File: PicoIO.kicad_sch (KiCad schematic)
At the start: 14 parts

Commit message: PCB revision 1 (NOT READY FOR USE)
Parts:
- removed J?: Conn_01x07, symbol Connector_Generic:Conn_01x07
- added J12: Conn_01x06, Connector_JST:JST_XH_B6B-XH-A_1x06_P2.50mm_Vertical, symbol Connector_Generic:Conn_01x06
- added R1, R10, R2, R3, R4, R5, R6, R7, R8, R9: 330, Resistor_SMD:R_0805_2012Metric_Pad1.20x1.40mm_HandSolder, symbol Device:R
- J1, J10, J11, J2, J3, J4, J5, J6, J7, J8, J9: renamed from J?; footprint (none) -> Connector_JST:JST_XH_B3B-XH-A_1x03_P2.50mm_Vertical
- J13: renamed from J?; footprint (none) -> Connector_PinHeader_2.54mm:PinHeader_1x03_P2.54mm_Vertical
- U1: renamed from U?; footprint RPi_Pico:RPi_Pico_SMD_TH -> MCU_RaspberryPi_and_Boards:RPi_Pico_SMD_TH
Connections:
- net EXP1 is gone; now on net P1 UR LED: U1.16 (GPIO12)
- net EXP2 is gone; now on net P1 UR: U1.17 (GPIO13)
- net EXP3 is gone; now on net GND: U1.29 (GPIO22)
- net +3V3: now also J12.3 (Pin_3)
- net +5V: now also J12.2 (Pin_2)
- net GND: now also J1.1 (Pin_1), J10.1 (Pin_1), J11.1 (Pin_1), J13.1 (Pin_1), J2.1 (Pin_1), J3.1 (Pin_1), J4.1 (Pin_1), J5.1 (Pin_1), J6.1 (Pin_1), J7.1 (Pin_1), J8.1 (Pin_1), J9.1 (Pin_1), U1.42 (GND), J12.1 (Pin_1); no longer J1.3 (Pin_3), J10.3 (Pin_3), J11.3 (Pin_3), J13.2 (Pin_2), J2.3 (Pin_3), J3.3 (Pin_3), J4.3 (Pin_3), J5.3 (Pin_3), J6.3 (Pin_3), J7.3 (Pin_3), J8.3 (Pin_3), J9.3 (Pin_3)
- net P1 CN: now also J3.3 (Pin_3), U1.12 (GPIO9); no longer J3.1 (Pin_1), U1.14 (GPIO10)
- net P1 CN LED: now also U1.11 (GPIO8), R3.1; no longer J3.2 (Pin_2), U1.15 (GPIO11)
- net P1 DL: now also J1.3 (Pin_3), U1.2 (GPIO1); no longer J1.1 (Pin_1), U1.25 (GPIO19)
- net P1 DL LED: now also U1.1 (GPIO0), R1.1; no longer J1.2 (Pin_2), U1.24 (GPIO18)
- net P1 DR: now also J5.3 (Pin_3), U1.26 (GPIO20); no longer J5.1 (Pin_1), U1.11 (GPIO8)
- net P1 DR LED: now also U1.27 (GPIO21), R5.1; no longer J5.2 (Pin_2), U1.12 (GPIO9)
- net P1 UL: now also J2.3 (Pin_3), U1.7 (GPIO5); no longer J2.1 (Pin_1), U1.27 (GPIO21)
- net P1 UL LED: now also U1.6 (GPIO4), R2.1; no longer J2.2 (Pin_2), U1.26 (GPIO20)
- net P1 UR: now also J4.3 (Pin_3); no longer J4.1 (Pin_1), U1.9 (GPIO6)
- net P1 UR LED: now also R4.1; no longer J4.2 (Pin_2), U1.10 (GPIO7)
- net P2 CN: now also J8.3 (Pin_3), U1.15 (GPIO11); no longer J8.1 (Pin_1), U1.4 (GPIO2)
- net P2 CN LED: now also U1.14 (GPIO10), R8.1; no longer J8.2 (Pin_2), U1.5 (GPIO3)
- net P2 DL: now also J6.3 (Pin_3), U1.5 (GPIO3); no longer J6.1 (Pin_1), U1.22 (GPIO17)
- net P2 DL LED: now also U1.4 (GPIO2), R6.1; no longer J6.2 (Pin_2), U1.21 (GPIO16)
- net P2 DR: now also J10.3 (Pin_3), U1.24 (GPIO18); no longer J10.1 (Pin_1), U1.6 (GPIO4)
- net P2 DR LED: now also U1.25 (GPIO19), R10.1; no longer J10.2 (Pin_2), U1.7 (GPIO5)
- net P2 UL: now also J7.3 (Pin_3), U1.10 (GPIO7); no longer J7.1 (Pin_1), U1.32 (GPIO27_ADC1)
- net P2 UL LED: now also U1.9 (GPIO6), R7.1; no longer J7.2 (Pin_2), U1.31 (GPIO26_ADC0)
- net P2 UR: now also J9.3 (Pin_3), U1.20 (GPIO15); no longer J9.1 (Pin_1), U1.1 (GPIO0)
- net P2 UR LED: now also U1.19 (GPIO14), R9.1; no longer J9.2 (Pin_2), U1.2 (GPIO1)
- net SERVICE: now also J11.3 (Pin_3), U1.21 (GPIO16); no longer J11.2 (Pin_2), U1.19 (GPIO14)
- net SWCLK: now also J13.2 (Pin_2), U1.41 (SWCLK); no longer J13.1 (Pin_1)
- net SWDIO: now also U1.43 (SWDIO)
- net TEST: now also J11.2 (Pin_2), U1.22 (GPIO17); no longer J11.1 (Pin_1), U1.20 (GPIO15)
- net EXP4 renamed ADC2
- net ADC2: now also J12.6 (Pin_6)
- new net: J8.2 (Pin_2), R8.2
- new net: J5.2 (Pin_2), R5.2
- new net: J7.2 (Pin_2), R7.2
- new net: J4.2 (Pin_2), R4.2
- new net: J10.2 (Pin_2), R10.2
- new net: J9.2 (Pin_2), R9.2
- new net: J6.2 (Pin_2), R6.2
- new net: J3.2 (Pin_2), R3.2
- new net: J1.2 (Pin_2), R1.2
- new net: J2.2 (Pin_2), R2.2
- new net ADC0: J12.4 (Pin_4), U1.31 (GPIO26_ADC0)
- new net ADC1: J12.5 (Pin_5), U1.32 (GPIO27_ADC1)
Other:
- moved on the sheet: J10, J11, J13, J6, J7, J8, J9

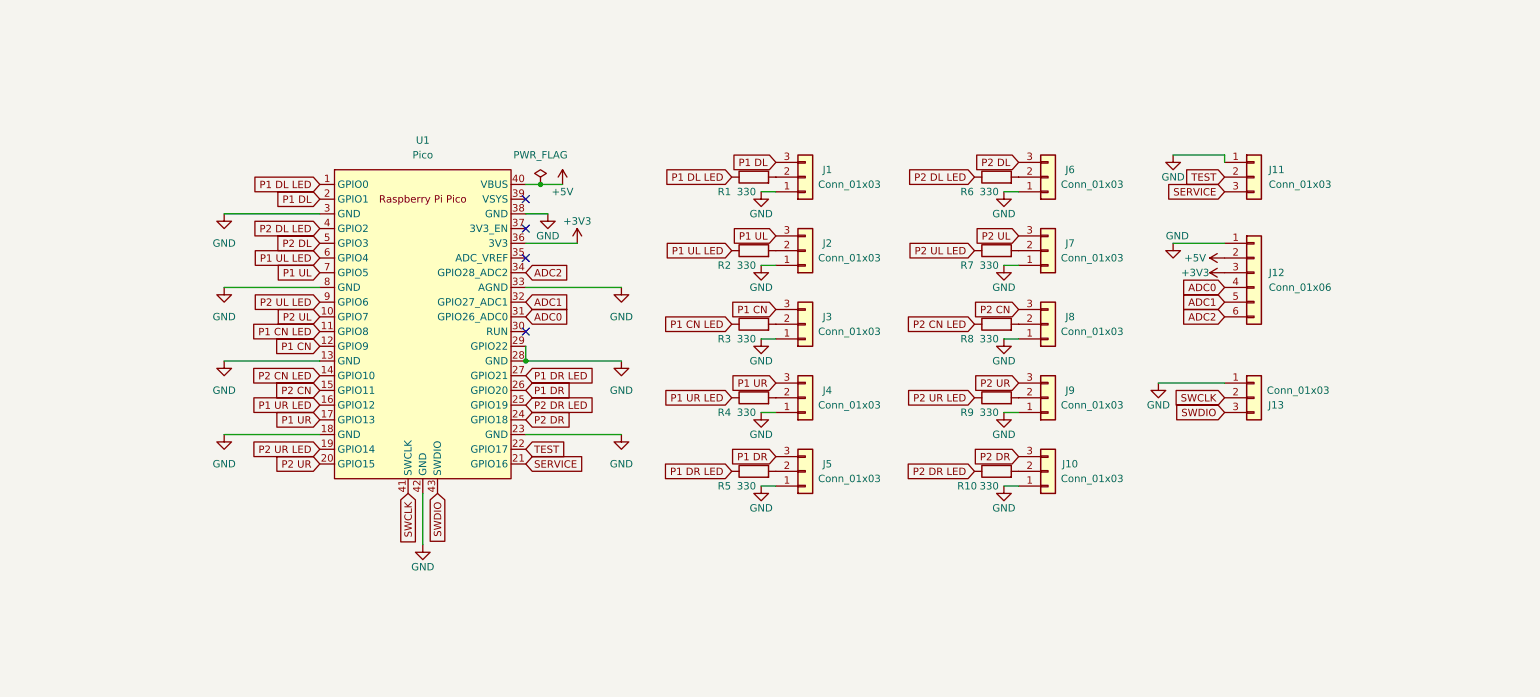
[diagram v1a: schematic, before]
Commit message: Add MOSFETs, move to 4 pin JST, DRC passed
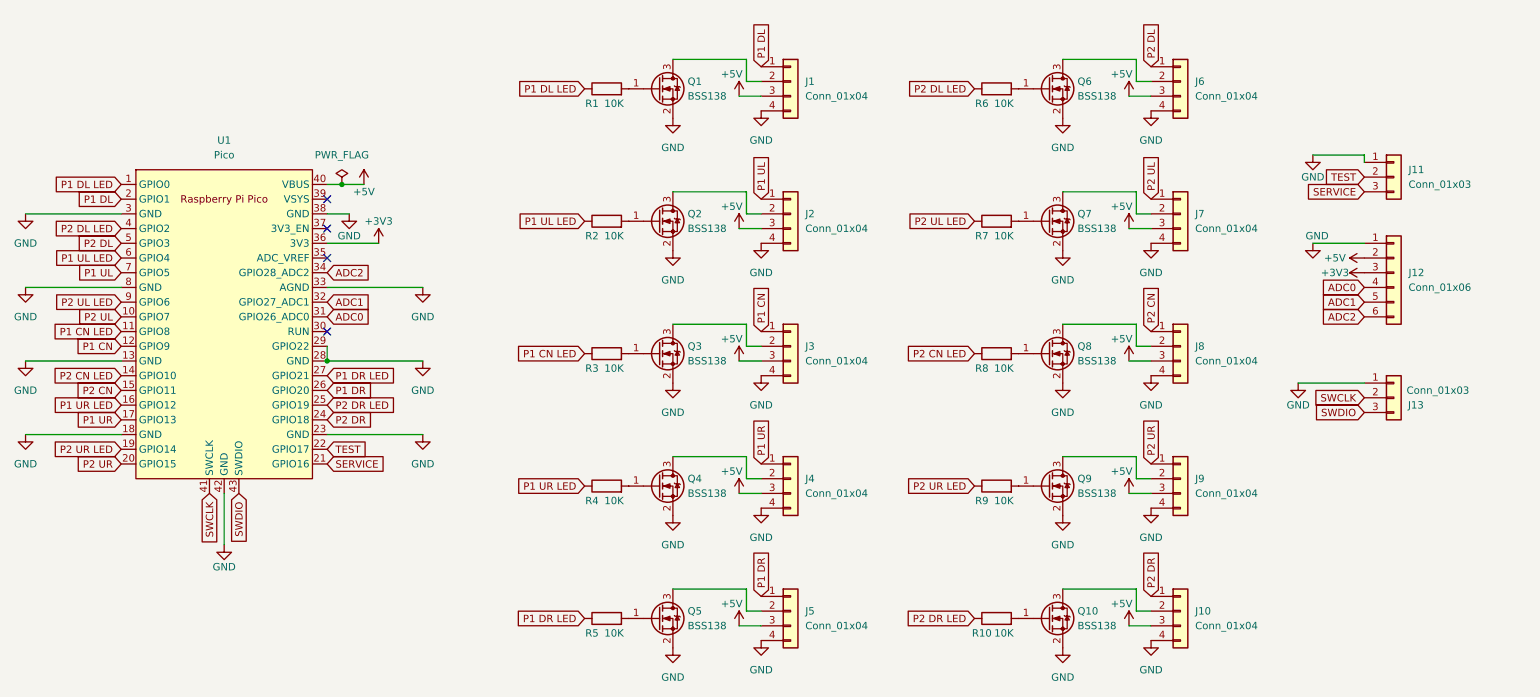
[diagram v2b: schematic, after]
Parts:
- removed J1, J10, J2, J3, J4, J5, J6, J7, J8, J9: Conn_01x03, Connector_JST:JST_XH_B3B-XH-A_1x03_P2.50mm_Vertical, symbol Connector_Generic:Conn_01x03
- added J1, J10, J2, J3, J4, J5, J6, J7, J8, J9: Conn_01x04, Connector_JST:JST_XH_B4B-XH-A_1x04_P2.50mm_Vertical, symbol Connector_Generic:Conn_01x04
- added Q1, Q10, Q2, Q3, Q4, Q5, Q6, Q7, Q8, Q9: BSS138, Package_TO_SOT_SMD:SOT-23, symbol Transistor_FET:BSS138
- R1, R10, R2, R3, R4, R5, R6, R7, R8, R9: value 330 -> 10K
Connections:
- net +5V: now also J1.3 (Pin_3), J10.3 (Pin_3), J2.3 (Pin_3), J3.3 (Pin_3), J4.3 (Pin_3), J5.3 (Pin_3), J6.3 (Pin_3), J7.3 (Pin_3), J8.3 (Pin_3), J9.3 (Pin_3)
- net GND: now also J1.4 (Pin_4), J10.4 (Pin_4), J2.4 (Pin_4), J3.4 (Pin_4), J4.4 (Pin_4), J5.4 (Pin_4), J6.4 (Pin_4), J7.4 (Pin_4), J8.4 (Pin_4), J9.4 (Pin_4), Q1.2 (S), Q10.2 (S), Q2.2 (S), Q3.2 (S), Q4.2 (S), Q5.2 (S), Q6.2 (S), Q7.2 (S), Q8.2 (S), Q9.2 (S)
- net P1 CN: now also J3.1 (Pin_1)
- net P1 DL: now also J1.1 (Pin_1)
- net P1 DR: now also J5.1 (Pin_1)
- net P1 UL: now also J2.1 (Pin_1)
- net P1 UR: now also J4.1 (Pin_1)
- net P2 CN: now also J8.1 (Pin_1)
- net P2 DL: now also J6.1 (Pin_1)
- net P2 DR: now also J10.1 (Pin_1)
- net P2 UL: now also J7.1 (Pin_1)
- net P2 UR: now also J9.1 (Pin_1)
- net at R8.2: now also Q8.1 (G)
- net at R5.2: now also Q5.1 (G)
- net at R7.2: now also Q7.1 (G)
- net at R4.2: now also Q4.1 (G)
- net at R10.2: now also Q10.1 (G)
- net at R9.2: now also Q9.1 (G)
- net at R6.2: now also Q6.1 (G)
- net at R3.2: now also Q3.1 (G)
- net at R1.2: now also Q1.1 (G)
- net at R2.2: now also Q2.1 (G)
- new net: J2.2 (Pin_2), Q2.3 (D)
- new net: J3.2 (Pin_2), Q3.3 (D)
- new net: J8.2 (Pin_2), Q8.3 (D)
- new net: J4.2 (Pin_2), Q4.3 (D)
- new net: J10.2 (Pin_2), Q10.3 (D)
- new net: J1.2 (Pin_2), Q1.3 (D)
- new net: J6.2 (Pin_2), Q6.3 (D)
- new net: J5.2 (Pin_2), Q5.3 (D)
- new net: J7.2 (Pin_2), Q7.3 (D)
- new net: J9.2 (Pin_2), Q9.3 (D)
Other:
- moved on the sheet: J11, J12, J13, U1

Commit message: External LED power, some routing/aesthetic changes
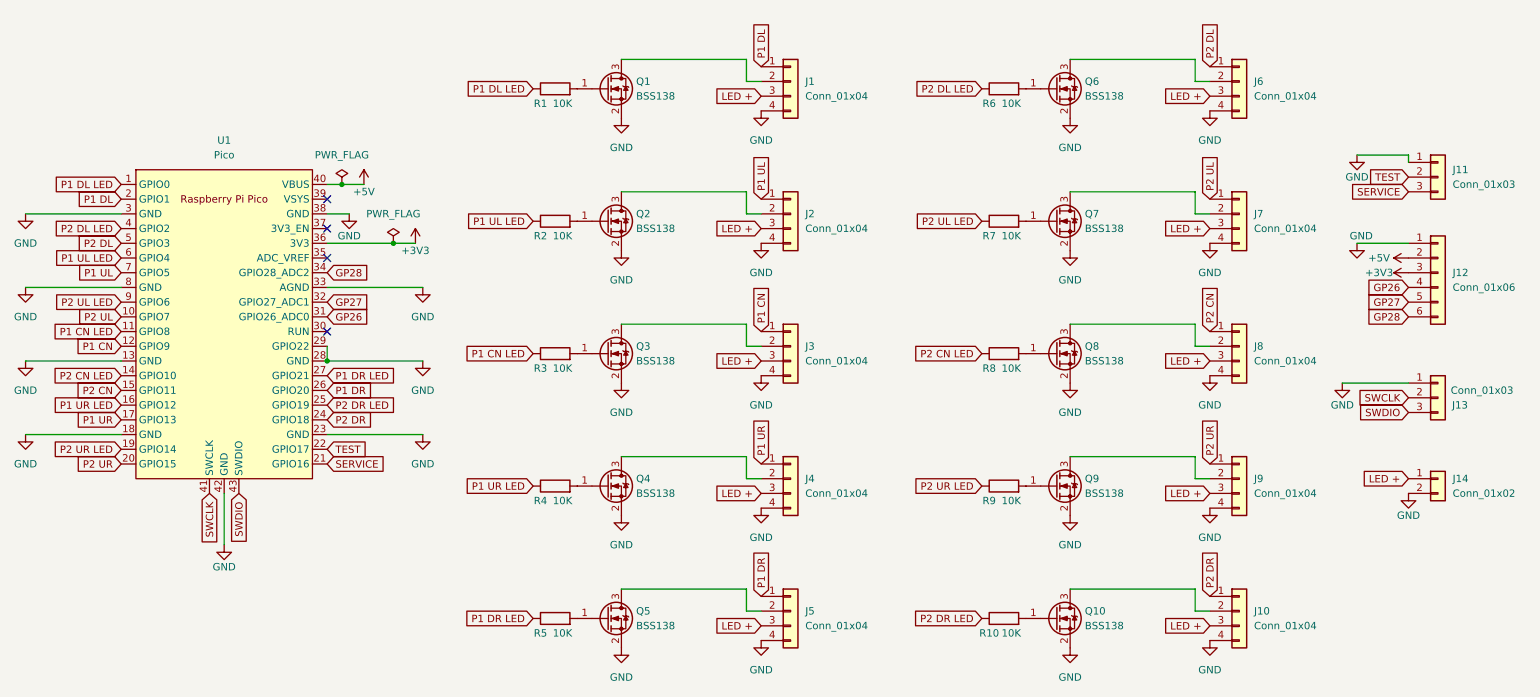
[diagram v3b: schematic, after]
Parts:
- added J14: Conn_01x02, Connector_JST:JST_XH_B2B-XH-A_1x02_P2.50mm_Vertical, symbol Connector_Generic:Conn_01x02
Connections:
- net +5V: no longer J1.3 (Pin_3), J10.3 (Pin_3), J2.3 (Pin_3), J3.3 (Pin_3), J4.3 (Pin_3), J5.3 (Pin_3), J6.3 (Pin_3), J7.3 (Pin_3), J8.3 (Pin_3), J9.3 (Pin_3)
- net GND: now also J14.2 (Pin_2)
- net ADC0 renamed GP26
- net ADC1 renamed GP27
- net ADC2 renamed GP28
- new net LED +: J1.3 (Pin_3), J10.3 (Pin_3), J14.1 (Pin_1), J2.3 (Pin_3), J3.3 (Pin_3), J4.3 (Pin_3), J5.3 (Pin_3), J6.3 (Pin_3), J7.3 (Pin_3), J8.3 (Pin_3), J9.3 (Pin_3)
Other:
- moved on the sheet: J10, J11, J12, J13, J6, J7, J8, J9, Q1, Q10, Q2, Q3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
